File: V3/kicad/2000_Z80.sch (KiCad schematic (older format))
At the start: 0 parts

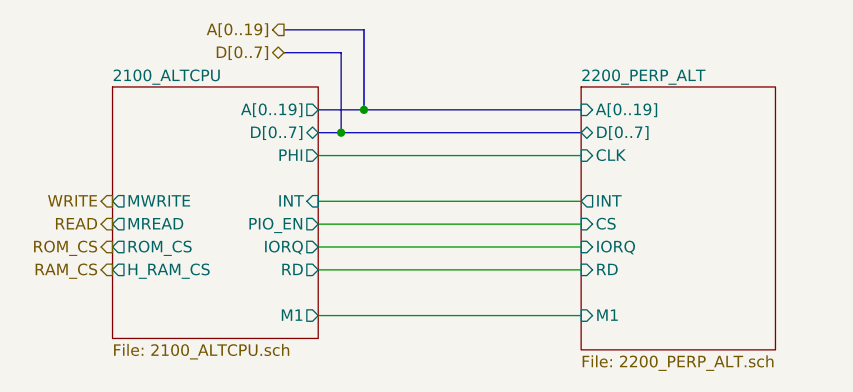
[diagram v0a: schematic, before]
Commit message: 3 1 1 m memory (#15)
* moved EEPROM files to /old

* Reworking 3.0 board

* changed footprint on RAM chip

* cleared out old memory traces

* started on rerouting

* on to autoroute

* little more cleanup

* more cleanup

* ill let the autoroute do the rest

* reroute complete

* made PQFP leads fatter

* Updated GAL logic

* Design Rule Check

* Minor pcb touch up

* gerber files

* just totally redid the whole thing

* More rearranging

* added a few caps

* Routed ROM and RAM together

* more routing

* more routes

* A lot of disorganized changes

* 3.1 CSIO SPI Bus (#9)

* Updated SPI to use CPU signals

8 bit register chip controls CS lines

* Renamed and added caps to SD page

* Cleanup

* 3.1 Resistor Replacement (#10)

* First two R arrays

* Added one more r array

* added cap for SPI FF

* Extended cpu pads (#12)

* 3.1 fix sheet hierarchy (#13)

* Fixed Schematic Heirarchy issue

* some footprints re-added to board

* Add footprints added

* Minor changes

* 3.1 redraw cpu courtyard (#14)

* moved all crtyd lines to same place in file

* Duplicate lines were causing issues

* Added pin header for SPI lines

* routed last of non-bus lines

* attempted to route memory lines

* Added new symbol and footprint

* CTS0 no longer drives an LED

* Final cleanup before memory routing

* got CTS0 and RTS mixed up

* Removed extra led from board

* Updated signature

* small changes
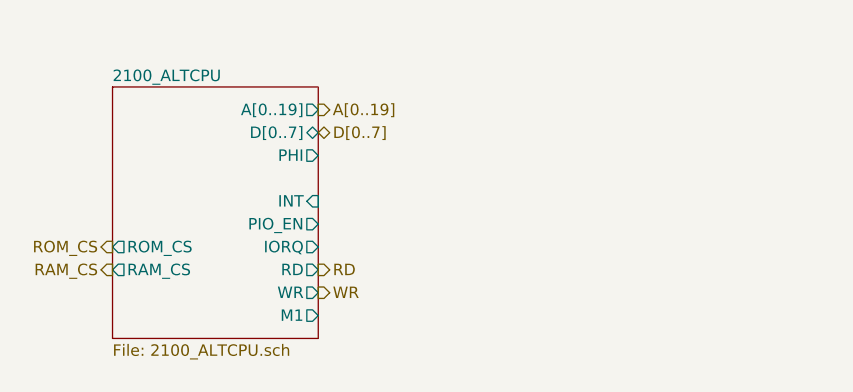
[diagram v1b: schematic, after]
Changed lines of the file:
@@
 $Descr A4 11693 8268
 encoding utf-8
-Sheet 3 9
+Sheet 3 7
 Title ""
 Date ""
@@
 Comment4 ""
 $EndDescr
-Wire Bus Line
-	5400 3150 5150 3150
-Wire Bus Line
-	5500 3050 5150 3050
-Text HLabel 5150 3150 0    50   3State ~ 0
+Text HLabel 5300 3500 2    50   3State ~ 0
 D[0..7]
-Wire Wire Line
-	5300 3600 6450 3600
-$Sheet
-S 6450 3300 850  1150
-U 61F28B7D
-F0 "2200_PERP_ALT" 50
-F1 "2200_PERP_ALT.sch" 50
-F2 "A[0..19]" I L 6450 3400 50
-F3 "D[0..7]" B L 6450 3500 50
-F4 "CLK" I L 6450 3600 50
-F5 "CS" I L 6450 3900 50
-F6 "IORQ" I L 6450 4000 50
-F7 "RD" I L 6450 4100 50
-F8 "M1" I L 6450 4300 50
-F9 "INT" O L 6450 3800 50
-$EndSheet
-Wire Wire Line
-	5300 4000 6450 4000
-Wire Wire Line
-	5300 4300 6450 4300
 $Sheet
 S 4400 3300 900  1100
@@
 F7 "ROM_CS" O L 4400 4000 50
 F8 "PIO_EN" O R 5300 3900 50
-F9 "MREAD" O L 4400 3900 50
-F10 "MWRITE" O L 4400 3800 50
-F11 "INT" I R 5300 3800 50
-F12 "H_RAM_CS" O L 4400 4100 50
-F13 "A[0..19]" O R 5300 3400 50
+F9 "INT" I R 5300 3800 50
+F10 "A[0..19]" O R 5300 3400 50
+F11 "RAM_CS" O L 4400 4100 50
+F12 "WR" O R 5300 4200 50
 $EndSheet
-Wire Wire Line
-	5300 4100 6450 4100
-Wire Wire Line
-	5300 3900 6450 3900
-Text HLabel 4400 3800 0    50   Output ~ 0
-WRITE
-Text HLabel 4400 3900 0    50   Output ~ 0
-READ
 Text HLabel 4400 4000 0    50   Output ~ 0
 ROM_CS
 Text HLabel 4400 4100 0    50   Output ~ 0
 RAM_CS
-Wire Wire Line
-	6450 3800 5300 3800
-Text HLabel 5150 3050 0    50   Output ~ 0
+Text HLabel 5300 3400 2    50   Output ~ 0
 A[0..19]
-Wire Bus Line
-	5300 3400 5500 3400
-Wire Bus Line
-	5300 3500 5400 3500
-Wire Bus Line
-	5400 3150 5400 3500
-Connection ~ 5400 3500
-Wire Bus Line
-	5400 3500 6450 3500
-Wire Bus Line
-	5500 3050 5500 3400
-Connection ~ 5500 3400
-Wire Bus Line
-	5500 3400 6450 3400
+Text HLabel 5300 4200 2    50   Output ~ 0
+WR
+Text HLabel 5300 4100 2    50   Output ~ 0
+RD
 $EndSCHEMATC
